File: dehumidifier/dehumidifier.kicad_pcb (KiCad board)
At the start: 2 copper layers, 27.9 x 45.2 mm, 17 parts, among them J1 Barrel_Jack_Switch, J2 Conn_01x07, J3 Conn_01x07, J4 Conn_01x03_Pin, J5 Conn_01x02_Pin, J6 Conn_01x04_Pin, J7 Conn_01x03_Pin, Q1 2N3904, Q2 Q_NMOS_GDS

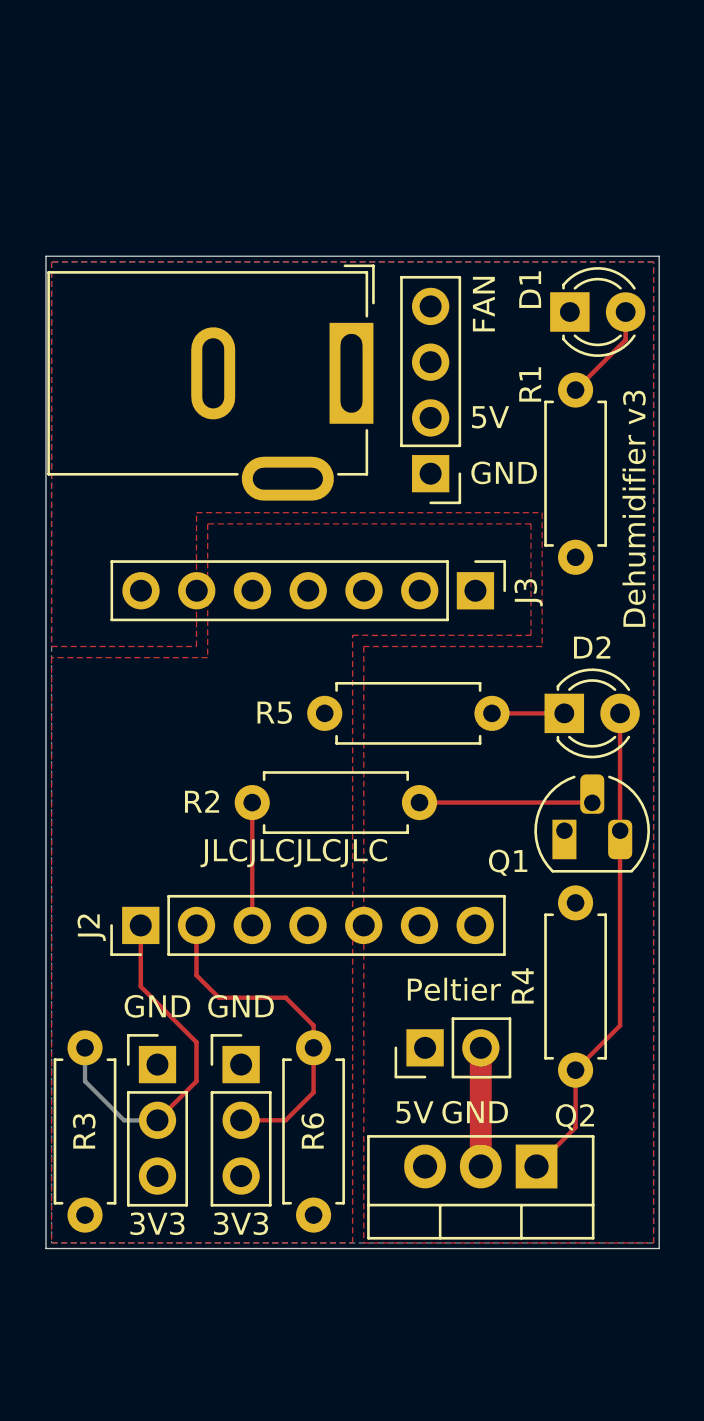
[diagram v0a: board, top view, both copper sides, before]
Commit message: adding current sensing
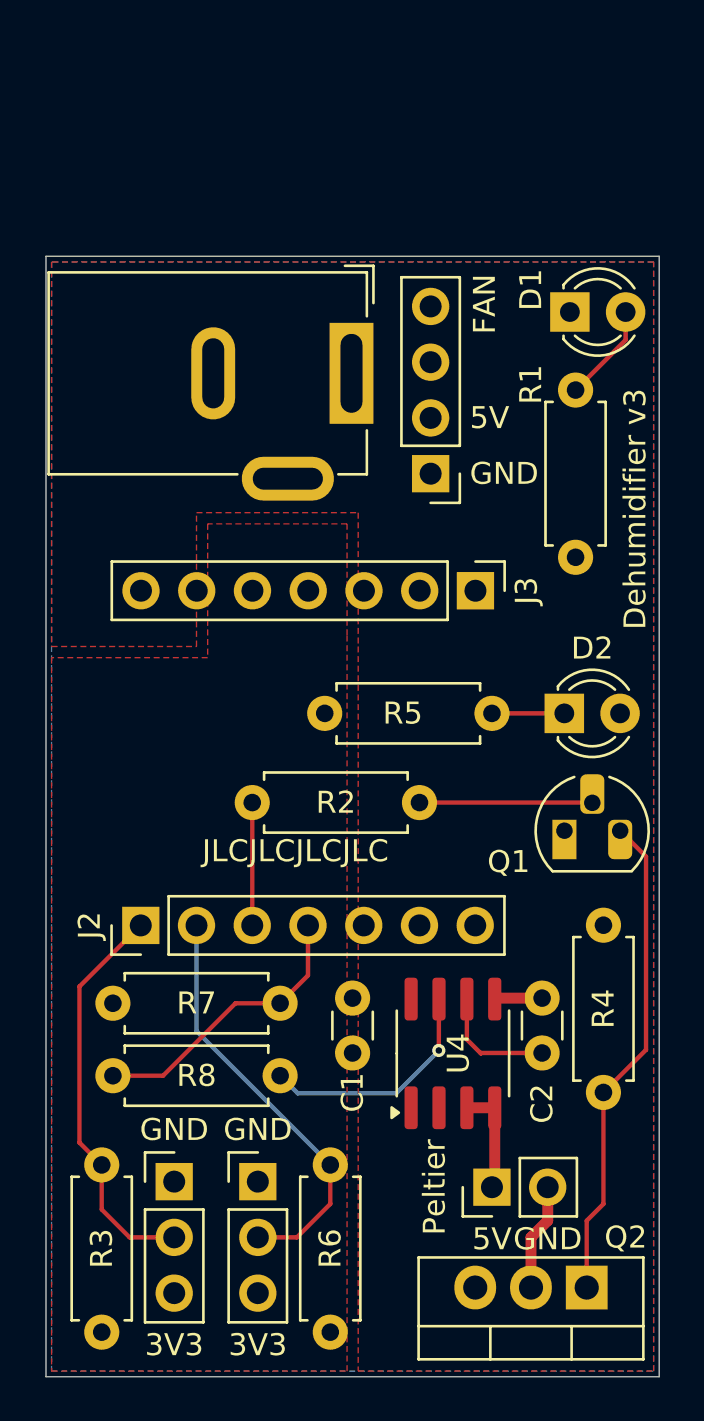
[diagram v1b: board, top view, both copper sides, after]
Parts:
- added C1: 100nF, Capacitor_THT:C_Disc_D3.0mm_W1.6mm_P2.50mm, F.Cu at (106.2, 86.1)
- added C2: 100nF, Capacitor_THT:C_Disc_D3.0mm_W1.6mm_P2.50mm, F.Cu at (114.8, 88.6)
- added R7: 10K, Resistor_THT:R_Axial_DIN0207_L6.3mm_D2.5mm_P7.62mm_Horizontal, F.Cu at (102.9, 86.4)
- added R8: 4K7, Resistor_THT:R_Axial_DIN0207_L6.3mm_D2.5mm_P7.62mm_Horizontal, F.Cu at (102.9, 89.7)
- added U4: ACS712xLCTR-05B, Package_SO:SOIC-8_3.9x4.9mm_P1.27mm, F.Cu at (110.7, 88.6)
- R6: value 4K7 -> 2K7
- moved J5 7.04 mm to (112.5, 94.7)
- moved Q2 5.97 mm to (116.8, 99.3)
- moved J4 5.39 mm to (98.0, 94.5)
- moved J7 5.39 mm to (101.9, 94.5)
- moved R3 5.39 mm to (94.7, 101.3)
- moved R6 5.39 mm to (105.2, 101.3)
- moved R4 1.63 mm to (117.6, 90.4)
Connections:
- J2 pad 4: unconnected-(J2-Pin_4-Pad4) -> CURRENT
- J5 pad 1: +5V -> Net-(J5-Pin_1)
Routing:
- net CURRENT: track 0.00 -> 13.1 mm
- net Net-(U4-VIOUT): track 0.00 -> 10.7 mm, vias 0 -> 1
- net Net-(U4-FILTER): track 0.00 -> 5.54 mm
- net Net-(J5-Pin_1): track 0.00 -> 4.94 mm
- net DS18B20_DATA: track 15.4 -> 19.1 mm
- net GND: track 0.00 -> 2.18 mm
- net DHT11_DATA: track 16.2 -> 18.4 mm
- net Net-(J5-Pin_2): track 5.41 -> 4.89 mm
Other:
- board size 27.9 x 45.2 mm -> 27.9 x 51.1 mm

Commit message: 12V for peltier
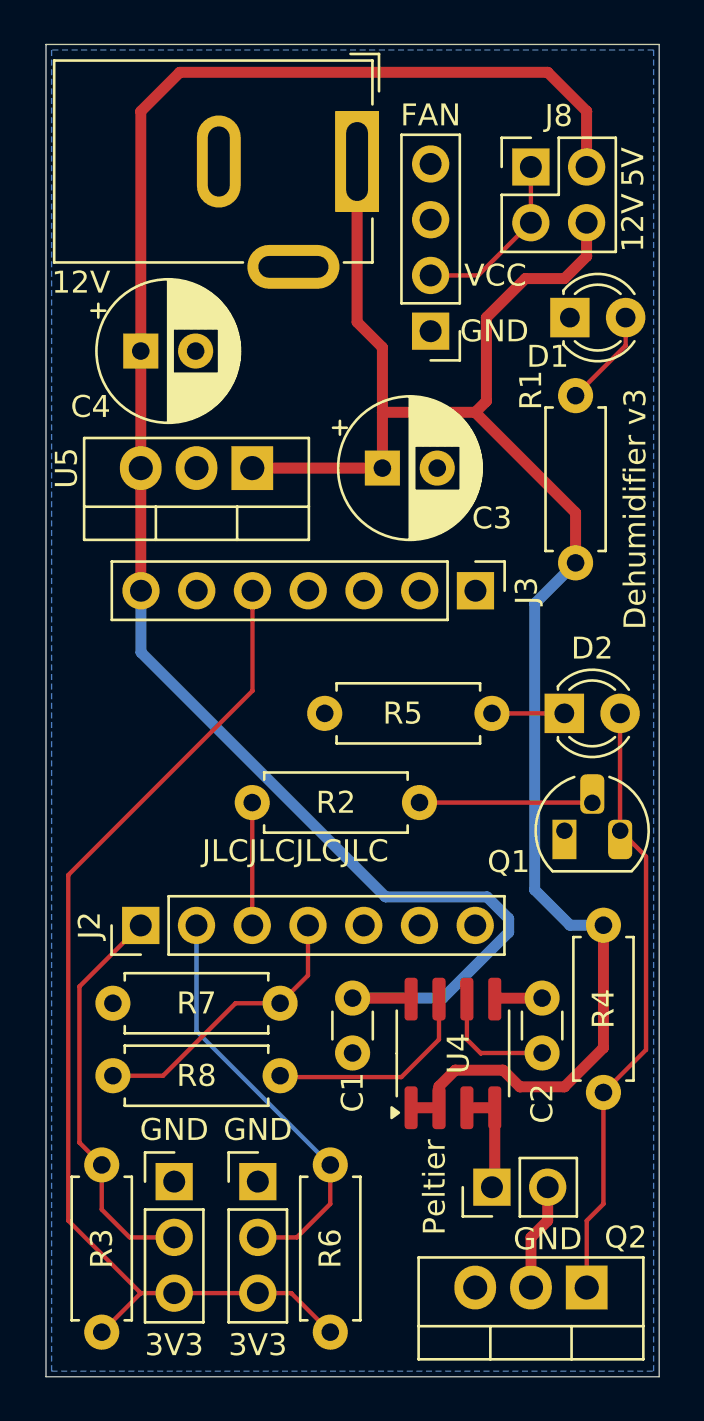
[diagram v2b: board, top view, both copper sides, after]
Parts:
- added C3: C_Polarized, Capacitor_THT:CP_Radial_D6.3mm_P2.50mm, F.Cu at (107.5, 62.0)
- added C4: C_Polarized, Capacitor_THT:CP_Radial_D6.3mm_P2.50mm, F.Cu at (96.5, 56.6)
- added J8: Conn_02x02_Odd_Even, Connector_PinHeader_2.54mm:PinHeader_2x02_P2.54mm_Vertical, F.Cu at (114.3, 48.3)
- added U5: LM78M05_TO220, Package_TO_SOT_THT:TO-220-3_Vertical, F.Cu at (101.6, 62.0)
- R1: value 470R -> 1K5
- moved J1 9.66 mm to (106.4, 48.0)
- moved J6 6.49 mm to (109.7, 55.7)
- moved D1 0.25 mm to (116.1, 55.1)
- moved R1 0.25 mm to (116.3, 58.7)
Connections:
- J1 pad 1: +5V -> +12V
- J6 pad 2: +5V -> V_FAN
- R1 pad 2: +5V -> +12V
- R4 pad 2: +5V -> +12V
- U4 pad 1: +5V -> +12V
- U4 pad 2: +5V -> +12V
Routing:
- net +5V: track 0.00 -> 82.4 mm
- net +12V: track 0.00 -> 81.3 mm
- net +3V3: track 0.00 -> 48.7 mm
- net V_FAN: track 0.00 -> 8.10 mm
- net Net-(D2-A): track 22.4 -> 27.8 mm
- net Net-(U4-VIOUT): track 10.7 -> 9.82 mm, vias 1 -> 0
- removed copper zone on F.Cu, net +3V3
- removed copper zone on F.Cu, net +5V
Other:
- board size 27.9 x 51.1 mm -> 27.9 x 60.7 mm
- board text added: "12V"
- board text added: "VCC"
